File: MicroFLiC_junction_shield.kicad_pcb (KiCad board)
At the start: 2 copper layers, 98 x 53.3 mm, 78 parts, among them P1 CONN_02X07, P2 CONN_02X04, P3 CONN_02X03, P4 CONN_02X06, P5 CONN_01X04, P6 CONN_02X08, Q1 TSM2314, Q2 TSM2314, Q3 TSM2314, SW1 SW_PUSH, U1 23LVC1024, U2 PCA9306, U3 DS1338, X1 32.768kHz

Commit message: Added MCU power control (MCUswitch.sch)
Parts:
- removed the PP12 at (215.4, 110.2)
- removed the PP13 at (212.9, 110.2)
- renumbered PP9 to PP10, PP10 to PP11, PP11 to PP12, PP14 to PP13, PP15 to PP14, PP16 to PP15, PP17 to PP16, PP18 to PP17, PP19 to PP18, PP20 to PP19, PP1 to PP2, PP21 to PP20, PP22 to PP21, PP23 to PP22, PP24 to PP23, PP25 to PP24, PP26 to PP25, PP27 to PP26, PP28 to PP27, PP29 to PP28, PP30 to PP29, PP2 to PP3, PP31 to PP30, PP33 to PP31, PP34 to PP31, PP35 to PP32, PP36 to PP33, PP39 to PP36, PP40 to PP39, PP3 to PP4, PP41 to PP40, PP42 to PP41, PP4 to PP5, PP5 to PP6, PP6 to PP7, PP7 to PP8, PP8 to PP9

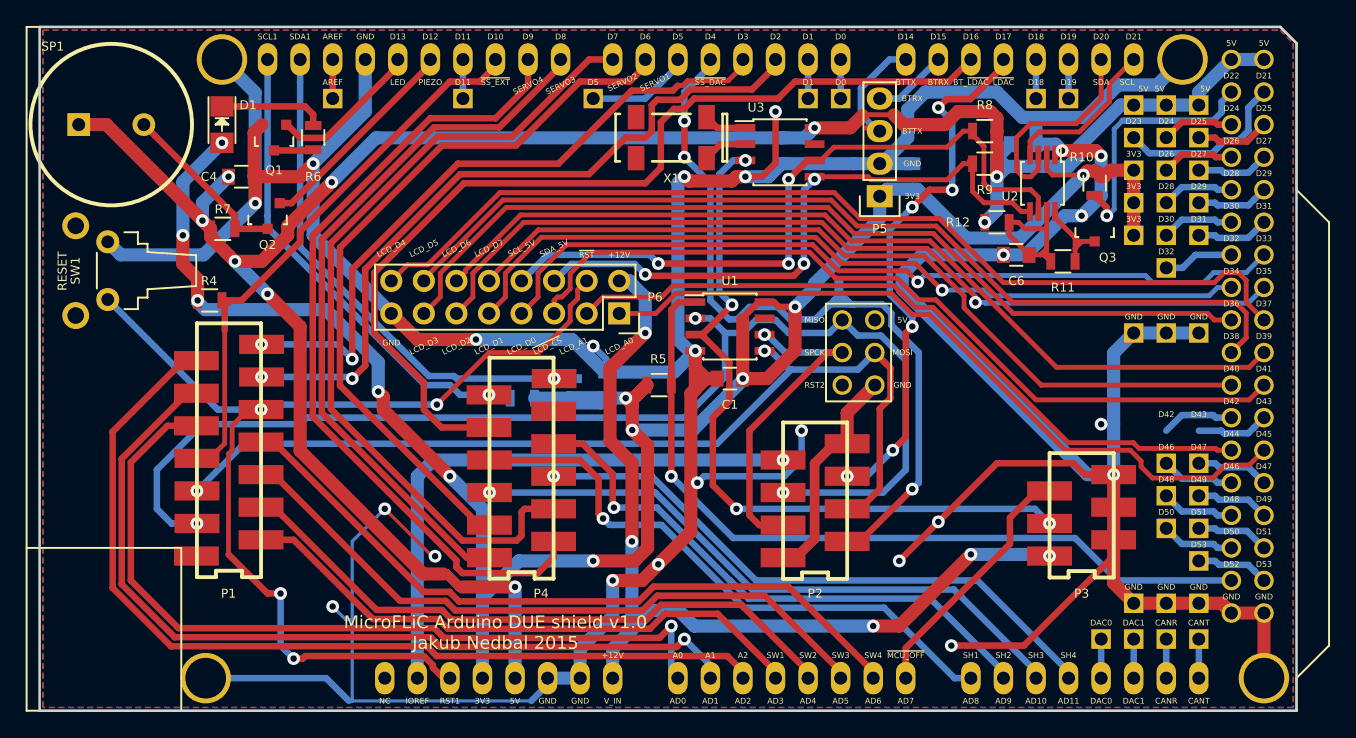
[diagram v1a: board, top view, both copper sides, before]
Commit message: Updated PCB for MCU switch, fixed SPCK connection, added correct angled connector for BT
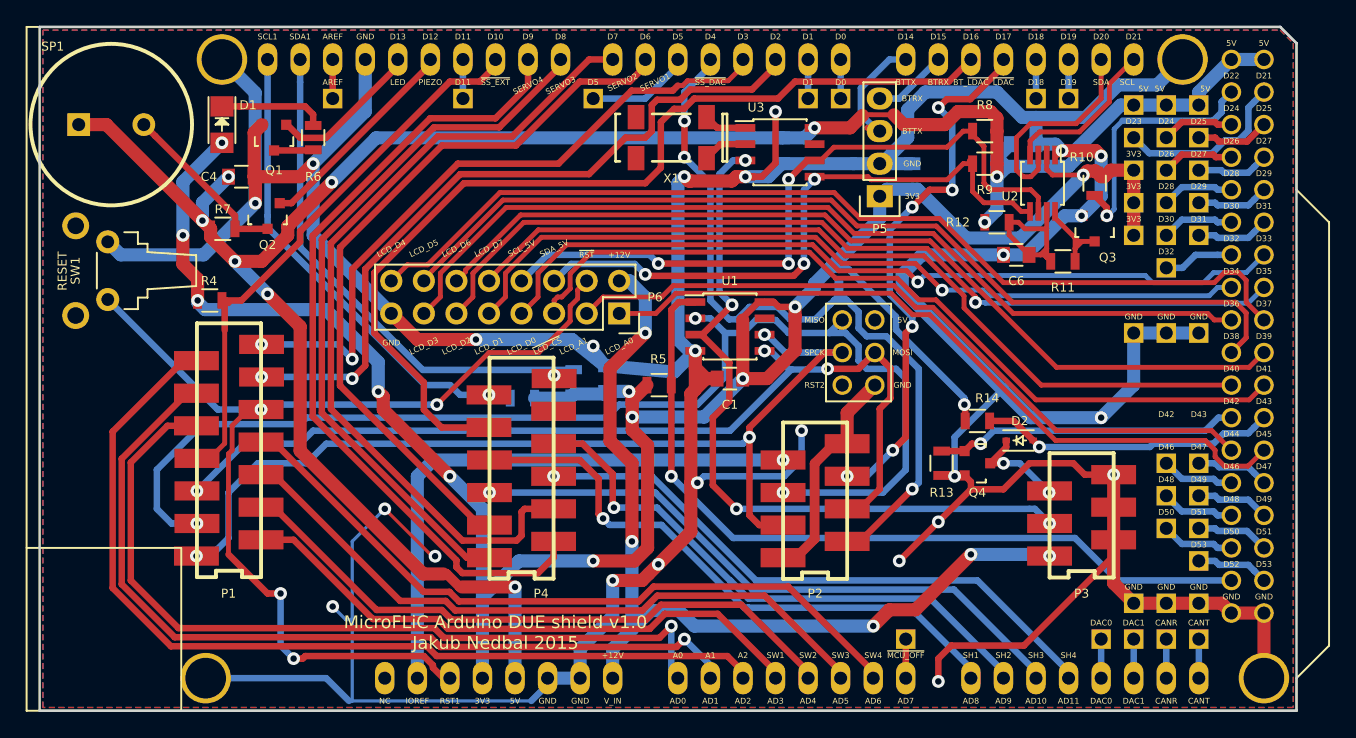
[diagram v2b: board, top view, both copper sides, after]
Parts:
- added D2: 1N4148, Diodes_SMD:SOD-323, F.Cu at (201.4, 111.0)
- added PP1: CONN_01X01, jakub:PIN_ARRAY_1, F.Cu at (192.5, 126.5)
- added Q4: TSM2314, TO_SOT_Packages_SMD:SOT-23, F.Cu at (198.1, 112.8)
- added R13: 100k, Resistors_SMD:R_0805, F.Cu at (195.3, 112.8)
- added R14: 100k, Resistors_SMD:R_0805, F.Cu at (198.1, 109.5)
- P1: value CONN_02X07 -> 14-way Micro-MaTch
- P2: value CONN_02X04 -> 8-way Micro-MaTch
- P3: value CONN_02X03 -> 6-way Micro-MaTch
- P4: value CONN_02X06 -> 12-way Micro-MaTch
- P5: value CONN_01X04 -> 1x4 Socket Strip R/A
- P6: value CONN_02X08 -> 2x8 socket strip
- R10, R3, R4, R5: value 47k -> 100k
- R11: value 180k -> 100k
- SW1: value SW_PUSH -> Tactile Switch R/A
- U1: value 23LVC1024 -> 23LCV1024
- U2: value PCA9306 -> PCA9306DP
- moved R2 0.70 mm to (166.6, 106.4)
- moved C3 0.49 mm to (169.2, 106.2)
- renumbered PP31 to PP33, PP32 to PP34, PP33 to PP35
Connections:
- P1 pad 1: (no net) -> /SPCK
- P3 pad 5: /~MCU_OFF -> /MCUswitch/~MCU_OFF
- P4 pad 10: (no net) -> Net-(P4-Pad10)
- SHIELD1 pad 42: /D42 -> /MCUswitch/PWR_OFF
- SHIELD1 pad 43: /D43 -> /MCUswitch/~SW_SENSE
- SHIELD1 pad 5V_6: (no net) -> Net-(SHIELD1-Pad5V_6)
- SHIELD1 pad AD7: /~MCU_OFF -> /AD7
- SHIELD1 pad NC: (no net) -> Net-(SHIELD1-PadNC)
- SHIELD1 pad RST2: (no net) -> Net-(SHIELD1-PadRST2)
- U1 pad 7: (no net) -> Net-(U1-Pad7)
- U3 pad 7: (no net) -> Net-(U3-Pad7)
- X1 pad 2: (no net) -> Net-(X1-Pad2)
- X1 pad 3: (no net) -> Net-(X1-Pad3)
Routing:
- net /SPCK: track 25.9 -> 75.2 mm, vias 1 -> 3
- net /MCUswitch/PWR_OFF: track 0.00 -> 23.7 mm, vias 0 -> 1
- net /MCUswitch/~SW_SENSE: track 0.00 -> 23.2 mm, vias 0 -> 1
- net /~MCU_OFF: track 19.8 -> 0.00 mm
- net +3V3: track 172.7 -> 186.8 mm, vias 11 -> 12
- net /MCUswitch/~MCU_OFF: track 0.00 -> 7.98 mm, vias 0 -> 2
- net /D43: track 5.67 -> 0.00 mm
- net /D42: track 5.67 -> 0.00 mm
- net GND: track 396.0 -> 400.1 mm, vias 24 -> 25
- net /AD7: track 0.00 -> 3.05 mm
- net /~SS_DAC: track 63.1 -> 60.8 mm
- net /MISO: track 95.7 -> 97.3 mm
- net /LCDandRTC/LCD_A0: track 58.1 -> 57.3 mm
- net /MOSI: track 74.7 -> 74.9 mm, vias 2 -> 3
